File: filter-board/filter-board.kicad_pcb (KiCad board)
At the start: 4 copper layers, 33 x 63.5 mm, 73 parts, among them J1 Conn_01x14_Male, J2 Conn_01x14_Male, U1 TL074, U2 TL074, U3 TL074, U4 SSI2164-Split

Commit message: wip
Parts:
- moved R29 15.8 mm to (75.7, 86.5)
- moved R31 8.39 mm to (70.1, 90.7)
- moved R28 3.22 mm to (58.9, 90.7)
- moved R21 2.82 mm to (72.9, 90.7)
- moved C10 2.32 mm to (61.7, 90.7)
- moved D4 0.51 mm to (72.6, 48.6)
- moved D6 0.46 mm to (64.3, 91.4)
- moved D5 0.38 mm to (67.3, 91.4)
- moved D8 0.25 mm to (75.7, 81.7)

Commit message: Filter board layout done
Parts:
- added G***: LOGO, LOGO, B.Cu at (64.8, 94.0)
- added REF**: OSHW-Logo2_7.3x6mm_SilkScreen, Symbol:OSHW-Logo2_7.3x6mm_SilkScreen, B.Cu at (64.8, 41.0)
- added kibuzzard-666D7707: G***, kibuzzard-666D7707, F.Cu at (64.8, 96.5)
- moved C4 5.97 mm to (69.7, 59.4), turned to 90 degrees
- moved C13 5.64 mm to (70.0, 64.1)
- moved R26 3.81 mm to (75.7, 69.0), turned to 90 degrees
- moved C9 3.06 mm to (73.9, 59.3)
- moved C12 2.79 mm to (53.8, 78.4)
- moved R32 2.79 mm to (56.6, 78.4)
- moved R27 2.79 mm to (72.9, 69.0)
- moved C10 1.27 mm to (60.5, 90.7)
- moved R21 1.02 mm to (71.9, 90.7)
- moved R28 0.89 mm to (58.0, 90.7)
- moved D5 0.76 mm to (66.5, 91.4)
- moved D6 0.76 mm to (63.5, 91.4)
- moved R31 0.76 mm to (69.3, 90.7)
- turned D7 to -90 degrees
- turned D8 to -90 degrees
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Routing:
- net /+9V: track 0.00 -> 105.6 mm, vias 0 -> 7
- net /CV Processing/Freq_CV_Biased: track 0.00 -> 70.9 mm, vias 0 -> 3
- net /UBP: track 0.00 -> 68.1 mm
- net /LP: track 0.00 -> 54.3 mm
- net Net-(R29-Pad2): track 0.00 -> 48.4 mm, vias 0 -> 2
- net /HP: track 0.00 -> 47.7 mm
- net /Freq_CV: track 0.00 -> 47.5 mm
- net /LBP: track 0.00 -> 42.7 mm, vias 0 -> 1
- net /+4.5V_Buf: track 0.00 -> 42.4 mm, vias 0 -> 14
- net /Res_CV: track 0.00 -> 41.9 mm
- net /+4.5V: track 0.00 -> 40.2 mm, vias 0 -> 1
- net /CV Processing/Res_CV_Biased: track 0.00 -> 35.4 mm, vias 0 -> 2
- net /In: track 0.00 -> 33.3 mm
- net /VCF/UBP-LBP: track 0.00 -> 30.8 mm
- net /+5.35V_Buf: track 0.00 -> 24.6 mm, vias 0 -> 2
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- added copper zone on B.Cu, net /+4.5V_Buf
- added copper zone on F.Cu, net /+9V
- added copper zone on In1.Cu, net /GND
- added copper zone on In2.Cu, net /GND
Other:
- board text added: "1"
- board text added: "10"
- board text added: "11"
- board text added: "12"
- board text added: "13"
- board text added: "14"
- board text added: "2"
- board text added: "3"
- board text added: "4"
- board text added: "5"
- board text added: "6"
- board text added: "7"
- board text added: "8"
- board text added: "9"
- board text added: "JLCJLCJLCJLC"
- board text added: "pedalmarkt.com"

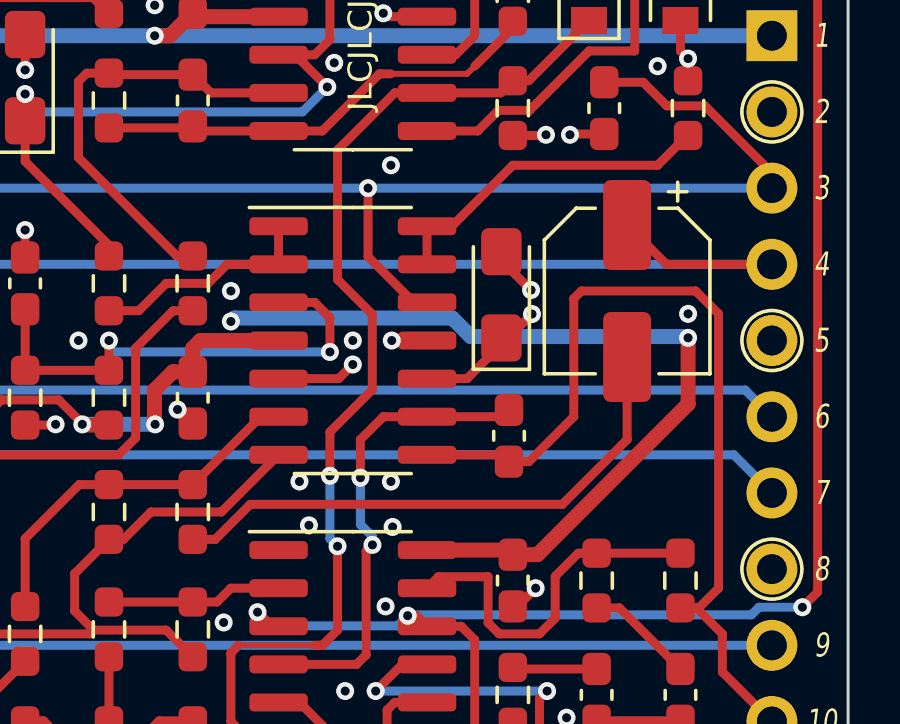
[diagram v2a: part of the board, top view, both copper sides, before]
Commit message: Follower schem done
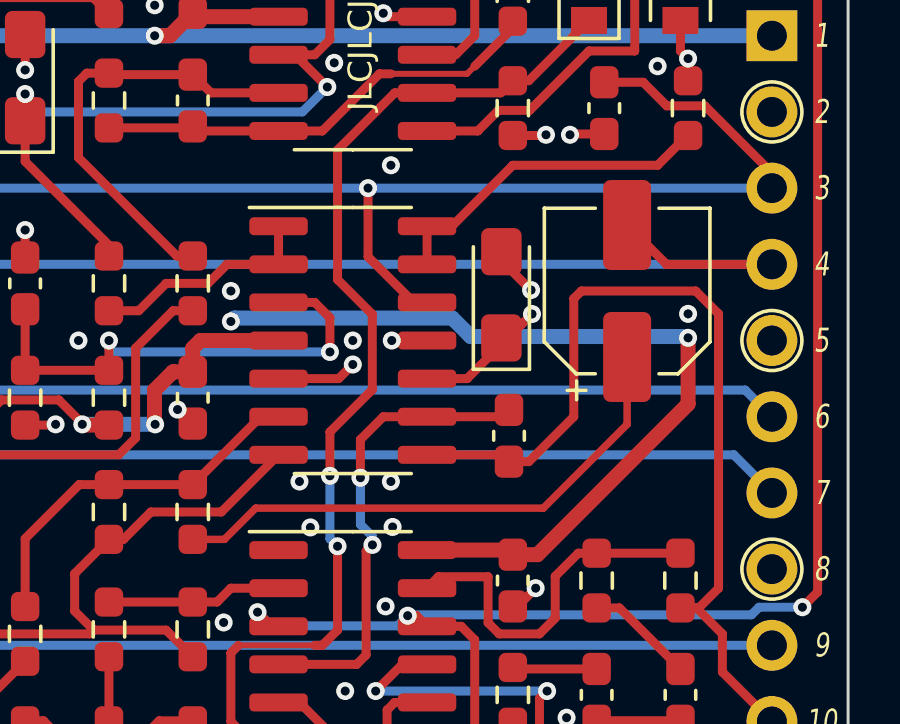
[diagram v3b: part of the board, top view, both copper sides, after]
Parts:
- turned C9 to 90 degrees
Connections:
- C9 pad 1: /In -> Net-(R14-Pad1)
- C9 pad 2: Net-(C9-Pad2) -> /In
- R14 pad 1: Net-(C9-Pad2) -> Net-(R14-Pad1)
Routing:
- net Net-(C9-Pad2): track 18.6 -> 0.00 mm
- net Net-(R14-Pad1): track 0.00 -> 18.3 mm
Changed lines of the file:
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@@
   (net 10 "Net-(C7-Pad2)")
   (net 11 "/In")
-  (net 12 "Net-(C9-Pad2)")
+  (net 12 "Net-(R14-Pad1)")
   (net 13 "Net-(C10-Pad1)")
   (net 14 "/VCF/UBP-LBP")
@@
   )
   (footprint "Capacitor_SMD:CP_Elec_5x5.4" (layer "F.Cu")
-    (at 73.914 59.309 -90)
+    (at 73.914 59.309 90)
     (descr "SMD capacitor, aluminum electrolytic, Nichicon, 5.0x5.4mm")
     (tags "capacitor electrolytic")
@@
     (fp_line (start -2.65 -1.65) (end -1.65 -2.65) (layer "F.Fab") (width 0.1))
     (fp_circle (center 0 0) (end 2.5 0) (layer "F.Fab") (width 0.1) (fill none))
-    (pad "1" smd roundrect (at -2.2 0 270) (size 3 1.6) (layers "F.Cu" "F.Paste" "F.Mask") (roundrect_rratio 0.15625)
+    (pad "1" smd roundrect (at -2.2 0 90) (size 3 1.6) (layers "F.Cu" "F.Paste" "F.Mask") (roundrect_rratio 0.15625)
+      (net 12 "Net-(R14-Pad1)") (pintype "passive"))
+    (pad "2" smd roundrect (at 2.2 0 90) (size 3 1.6) (layers "F.Cu" "F.Paste" "F.Mask") (roundrect_rratio 0.15625)
       (net 11 "/In") (pintype "passive"))
-    (pad "2" smd roundrect (at 2.2 0 270) (size 3 1.6) (layers "F.Cu" "F.Paste" "F.Mask") (roundrect_rratio 0.15625)
-      (net 12 "Net-(C9-Pad2)") (pintype "passive"))
     (model "${KICAD6_3DMODEL_DIR}/Capacitor_SMD.3dshapes/CP_Elec_5x5.4.wrl"
       (offset (xyz 0 0 0))
@@
     (fp_line (start 0.8 -0.4125) (end 0.8 0.4125) (layer "F.Fab") (width 0.1))
     (pad "1" smd roundrect (at -0.9125 0 90) (size 0.975 0.95) (layers "F.Cu" "F.Paste" "F.Mask") (roundrect_rratio 0.25)
-      (net 12 "Net-(C9-Pad2)") (pintype "passive"))
+      (net 12 "Net-(R14-Pad1)") (pintype "passive"))
     (pad "2" smd roundrect (at 0.9125 0 90) (size 0.975 0.95) (layers "F.Cu" "F.Paste" "F.Mask") (roundrect_rratio 0.25)
       (net 40 "Net-(R13-Pad2)") (pintype "passive"))
@@
     (attr board_only exclude_from_pos_files exclude_from_bom)
     (fp_text reference "kibuzzard-666D7707" (at 0 -5.11175) (layer "F.SilkS") hide
-      (effects (font (size 0 0)))
+      (effects (font (size 0 0) (thickness 0.15)))
     )
     (fp_text value "G***" (at 0 5.11175) (layer "F.SilkS") hide
-      (effects (font (size 0 0)))
+      (effects (font (size 0 0) (thickness 0.15)))
     )
     (fp_poly (pts
@@
   (via (at 72.009 54.102) (size 0.6) (drill 0.3) (layers "F.Cu" "B.Cu") (net 1))
   (via (at 70.104 42.418) (size 0.6) (drill 0.3) (layers "F.Cu" "B.Cu") (net 1))
-  (via (at 63.3085 67.1205) (size 0.6) (drill 0.3) (layers "F.Cu" "B.Cu") (free) (net 1))
+  (via (at 63.355289 67.189616) (size 0.6) (drill 0.3) (layers "F.Cu" "B.Cu") (free) (net 1))
   (via (at 53.848 57.277) (size 0.6) (drill 0.3) (layers "F.Cu" "B.Cu") (net 1))
   (via (at 55.118 81.661) (size 0.6) (drill 0.3) (layers "F.Cu" "B.Cu") (free) (net 1))
@@
   (segment (start 70.104 50.546) (end 70.104 50.3155) (width 0.3) (layer "F.Cu") (net 10))
   (segment (start 68.58 52.07) (end 66.04 52.07) (width 0.2) (layer "F.Cu") (net 10))
-  (segment (start 78.74 58.42) (end 75.225 58.42) (width 0.3) (layer "F.Cu") (net 11))
   (segment (start 75.225 58.42) (end 73.914 57.109) (width 0.3) (layer "F.Cu") (net 11))
+  (segment (start 78.74 58.42) (end 75.225 58.42) (width 0.3) (layer "F.Cu") (net 11))
   (segment (start 50.8 58.42) (end 78.74 58.42) (width 0.3) (layer "B.Cu") (net 11))
-  (segment (start 61.351106 66.421) (end 60.184606 67.5875) (width 0.3) (layer "F.Cu") (net 12))
-  (segment (start 71.755 66.421) (end 61.351106 66.421) (width 0.3) (layer "F.Cu") (net 12))
-  (segment (start 60.184606 67.5875) (end 59.436 67.5875) (width 0.3) (layer "F.Cu") (net 12))
-  (segment (start 73.914 64.262) (end 71.755 66.421) (width 0.3) (layer "F.Cu") (net 12))
-  (segment (start 73.914 61.509) (end 73.914 64.262) (width 0.3) (layer "F.Cu") (net 12))
+  (segment (start 73.914 61.509) (end 73.914 63.754) (width 0.25) (layer "F.Cu") (net 12))
+  (segment (start 73.914 63.754) (end 71.12 66.548) (width 0.25) (layer "F.Cu") (net 12))
+  (segment (start 61.5315 66.548) (end 60.492 67.5875) (width 0.25) (layer "F.Cu") (net 12))
+  (segment (start 60.492 67.5875) (end 59.436 67.5875) (width 0.25) (layer "F.Cu") (net 12))
+  (segment (start 71.12 66.548) (end 61.5315 66.548) (width 0.25) (layer "F.Cu") (net 12))
   (segment (start 60.5525 91.5405) (end 60.452 91.5405) (width 0.3) (layer "F.Cu") (net 13))
   (segment (start 57.277 90.678) (end 56.769 90.17) (width 0.3) (layer "F.Cu") (net 13))

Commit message: Pot Adapter v1rev1
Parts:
- added kibuzzard-666B0D3F: G***, kibuzzard-666B0D3F, B.Cu at (54.9, 50.8)
- added kibuzzard-666B0D4B: G***, kibuzzard-666B0D4B, B.Cu at (54.9, 53.3)
- added kibuzzard-666B0D4B: G***, kibuzzard-666B0D4B, B.Cu at (54.9, 61.0)
- added kibuzzard-666B0D4B: G***, kibuzzard-666B0D4B, B.Cu at (54.9, 76.2)
- added kibuzzard-666B0D4B: G***, kibuzzard-666B0D4B, B.Cu at (54.9, 83.8)
- added kibuzzard-666B0D4B: G***, kibuzzard-666B0D4B, B.Cu at (54.9, 68.6)
- added kibuzzard-666B0D54: G***, kibuzzard-666B0D54, B.Cu at (54.9, 55.9)
- added kibuzzard-666B0D65: G***, kibuzzard-666B0D65, B.Cu at (74.7, 50.8)
- added kibuzzard-666B0D69: G***, kibuzzard-666B0D69, B.Cu at (74.7, 83.8)
- added kibuzzard-666B0D69: G***, kibuzzard-666B0D69, B.Cu at (74.7, 76.2)
- added kibuzzard-666B0D69: G***, kibuzzard-666B0D69, B.Cu at (74.7, 61.0)
- added kibuzzard-666B0D69: G***, kibuzzard-666B0D69, B.Cu at (74.7, 68.6)
- added kibuzzard-666B0D69: G***, kibuzzard-666B0D69, B.Cu at (74.7, 53.3)
- added kibuzzard-666B0D6E: G***, kibuzzard-666B0D6E, B.Cu at (74.7, 55.9)
- added kibuzzard-6673DFE6: G***, kibuzzard-6673DFE6, B.Cu at (54.9, 58.4)
- added kibuzzard-6673E097: G***, kibuzzard-6673E097, B.Cu at (74.7, 58.4)
- added kibuzzard-6673E301: G***, kibuzzard-6673E301, B.Cu at (55.0, 71.1)
- added kibuzzard-6673E306: G***, kibuzzard-6673E306, B.Cu at (74.6, 71.1)
- added kibuzzard-6673E326: G***, kibuzzard-6673E326, B.Cu at (55.0, 81.3)
- added kibuzzard-6673E32C: G***, kibuzzard-6673E32C, B.Cu at (74.6, 81.3)
- added kibuzzard-6673E332: G***, kibuzzard-6673E332, B.Cu at (74.6, 78.7)
- added kibuzzard-6673E338: G***, kibuzzard-6673E338, B.Cu at (55.0, 78.7)
- added kibuzzard-6673E33D: G***, kibuzzard-6673E33D, B.Cu at (55.0, 73.7)
- added kibuzzard-6673E342: G***, kibuzzard-6673E342, B.Cu at (74.6, 73.7)
- added kibuzzard-6673E377: G***, kibuzzard-6673E377, B.Cu at (55.0, 63.5)
- added kibuzzard-6673E380: G***, kibuzzard-6673E380, B.Cu at (54.9, 66.0)
- added kibuzzard-6673E386: G***, kibuzzard-6673E386, B.Cu at (74.7, 66.0)
- added kibuzzard-6673E38A: G***, kibuzzard-6673E38A, B.Cu at (74.5, 63.5)
- J1, J2: moved to B.Cu
- turned J1 to 180 degrees
- turned J2 to 180 degrees
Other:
- board text added: "v1rev1"

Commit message: Filter board ordered
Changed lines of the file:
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@@
   (net 10 "Net-(C7-Pad2)")
   (net 11 "/In")
-  (net 12 "Net-(R14-Pad1)")
+  (net 12 "Net-(C9-Pad1)")
   (net 13 "Net-(C10-Pad1)")
   (net 14 "/VCF/UBP-LBP")
@@
     (fp_circle (center 0 0) (end 2.5 0) (layer "F.Fab") (width 0.1) (fill none))
     (pad "1" smd roundrect (at -2.2 0 90) (size 3 1.6) (layers "F.Cu" "F.Paste" "F.Mask") (roundrect_rratio 0.15625)
-      (net 12 "Net-(R14-Pad1)") (pintype "passive"))
+      (net 12 "Net-(C9-Pad1)") (pintype "passive"))
     (pad "2" smd roundrect (at 2.2 0 90) (size 3 1.6) (layers "F.Cu" "F.Paste" "F.Mask") (roundrect_rratio 0.15625)
       (net 11 "/In") (pintype "passive"))
@@
     (fp_line (start 1.6 0.8) (end 1.6 -0.8) (layer "F.Fab") (width 0.1))
     (fp_line (start 1.6 -0.8) (end -1.2 -0.8) (layer "F.Fab") (width 0.1))
-    (pad "1" smd roundrect (at -1.4375 0 90) (size 1.575 1.35) (layers "F.Cu" "F.Paste" "F.Mask") (roundrect_rratio 0.185185)
+    (pad "1" smd roundrect (at -1.4375 0 90) (size 1.575 1.35) (layers "F.Cu" "F.Paste" "F.Mask") (roundrect_rratio 0.1851851852)
       (net 4 "/+5.35V_Buf") (pintype "passive"))
-    (pad "2" smd roundrect (at 1.4375 0 90) (size 1.575 1.35) (layers "F.Cu" "F.Paste" "F.Mask") (roundrect_rratio 0.185185)
+    (pad "2" smd roundrect (at 1.4375 0 90) (size 1.575 1.35) (layers "F.Cu" "F.Paste" "F.Mask") (roundrect_rratio 0.1851851852)
       (net 1 "/GND") (pintype "passive"))
     (model "${KICAD6_3DMODEL_DIR}/Capacitor_Tantalum_SMD.3dshapes/CP_EIA-3216-18_Kemet-A.wrl"
@@
     (fp_line (start 0.8 -0.4125) (end 0.8 0.4125) (layer "F.Fab") (width 0.1))
     (pad "1" smd roundrect (at -0.9125 0 90) (size 0.975 0.95) (layers "F.Cu" "F.Paste" "F.Mask") (roundrect_rratio 0.25)
-      (net 12 "Net-(R14-Pad1)") (pintype "passive"))
+      (net 12 "Net-(C9-Pad1)") (pintype "passive"))
     (pad "2" smd roundrect (at 0.9125 0 90) (size 0.975 0.95) (layers "F.Cu" "F.Paste" "F.Mask") (roundrect_rratio 0.25)
       (net 40 "Net-(R13-Pad2)") (pintype "passive"))
@@
     (fp_line (start -1.6 -0.4) (end -1.6 0.8) (layer "F.Fab") (width 0.1))
     (fp_line (start -1.2 -0.8) (end -1.6 -0.4) (layer "F.Fab") (width 0.1))
-    (pad "1" smd roundrect (at -1.4375 0 90) (size 1.575 1.35) (layers "F.Cu" "F.Paste" "F.Mask") (roundrect_rratio 0.185185)
+    (pad "1" smd roundrect (at -1.4375 0 90) (size 1.575 1.35) (layers "F.Cu" "F.Paste" "F.Mask") (roundrect_rratio 0.1851851852)
       (net 5 "/+4.5V_Buf") (pintype "passive"))
-    (pad "2" smd roundrect (at 1.4375 0 90) (size 1.575 1.35) (layers "F.Cu" "F.Paste" "F.Mask") (roundrect_rratio 0.185185)
+    (pad "2" smd roundrect (at 1.4375 0 90) (size 1.575 1.35) (layers "F.Cu" "F.Paste" "F.Mask") (roundrect_rratio 0.1851851852)
       (net 1 "/GND") (pintype "passive"))
     (model "${KICAD6_3DMODEL_DIR}/Capacitor_Tantalum_SMD.3dshapes/CP_EIA-3216-18_Kemet-A.wrl"
